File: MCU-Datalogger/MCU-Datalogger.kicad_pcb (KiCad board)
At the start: 2 copper layers, 29 parts, among them J1 Conn_01x04_Pin, J2 Conn_01x04_Pin, J3 Conn_01x09_Pin, J4 Conn_02x03_Odd_Even, U1 24LC1025, U2 24LC1025, U3 DS1337S+, U4 ATMEGA328P-AU, Y1 32.768 KHz, Y2 16 MHz

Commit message: Added Outline in Edge.Cuts
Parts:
- moved H1 42.0 mm to (186.7, 81.8)
- moved H2 42.0 mm to (186.7, 87.6)
- moved H3 42.0 mm to (186.7, 93.3)
- moved H4 42.0 mm to (186.7, 99.1)
- moved C2 29.1 mm to (219.7, 95.5)
- moved C5 29.1 mm to (219.7, 104.5)
- moved D1 29.1 mm to (224.1, 99.7)
- moved D2 29.1 mm to (224.1, 102.8)
- moved R2 29.1 mm to (204.9, 83.4)
- moved R3 29.1 mm to (204.9, 86.3)
- moved R7 29.1 mm to (204.9, 98.1)
- moved U1 29.1 mm to (212.3, 94.4)
- moved U2 29.1 mm to (212.3, 101.2)
- moved C1 29.1 mm to (219.7, 92.5)
- moved C3 29.1 mm to (219.7, 98.5)
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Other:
- board outline added: 50.8 x 30.5 mm

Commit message: Place components
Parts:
- moved J3 99.7 mm to (134.0, 103.5), turned to 90 degrees
- moved BT1 92.5 mm to (132.1, 85.1)
- moved U3 84.2 mm to (139.7, 94.6)
- moved J2 84.0 mm to (159.4, 103.5), turned to 90 degrees
- moved Y1 80.9 mm to (132.1, 95.9), turned to 90 degrees
- moved U2 75.4 mm to (139.7, 80.6)
- moved C1 73.6 mm to (147.3, 78.7)
- moved U1 72.9 mm to (139.7, 87.6)
- moved C3 71.3 mm to (151.1, 78.7)
- moved R1 69.6 mm to (137.8, 99.1)
- moved C5 68.5 mm to (156.2, 78.7)
- moved D1 66.0 mm to (161.6, 78.7)
- moved J4 65.8 mm to (170.8, 83.2)
- moved R2 65.2 mm to (141.6, 99.1), turned to 180 degrees
- moved J1 63.4 mm to (173.4, 92.1)
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
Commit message: Refine outline
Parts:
- moved H3 1.61 mm to (130.0, 105.7)
- moved H4 1.52 mm to (175.3, 105.7)
- moved H1 1.14 mm to (130.0, 77.7)
- moved H2 1.02 mm to (175.3, 77.7)
- moved J3 0.65 mm to (134.6, 103.6)
- moved J2 0.64 mm to (160.0, 103.5)
- moved C1 0.34 mm to (147.6, 78.9)
- moved C3 0.32 mm to (151.4, 78.9)
- moved D1 0.31 mm to (161.8, 78.9)
- moved D2 0.31 mm to (166.0, 78.9)
- moved C5 0.30 mm to (156.5, 78.9)
- moved U2 0.13 mm to (139.7, 80.8)
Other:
- board size 50.8 x 30.5 mm -> 51.3 x 34 mm
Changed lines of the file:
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@@
   )
   (footprint "Package_SO:SOIC-8_5.23x5.23mm_P1.27mm" (layer "F.Cu")
-    (at 139.7 80.645)
+    (at 139.7254 80.7724)
     (descr "SOIC, 8 Pin (http://www.winbond.com/resource-files/w25q32jv%20revg%2003272018%20plus.pdf#page=68), generated with kicad-footprint-generator ipc_gullwing_generator.py")
     (tags "SOIC SO")
@@
     (property "ki_keywords" "I2C Serial EEPROM")
     (attr smd)
-    (fp_text reference "U2" (at 0 -3.56) (layer "F.SilkS")
+    (fp_text reference "U2" (at 0.3025 -3.56) (layer "F.SilkS")
         (effects (font (size 1 1) (thickness 0.15)))
     )
@@
   )
   (footprint "Connector_PinHeader_2.54mm:PinHeader_1x04_P2.54mm_Vertical" (layer "F.Cu")
-    (at 159.385 103.505 90)
+    (at 160.02 103.505 90)
     (descr "Through hole straight pin header, 1x04, 2.54mm pitch, single row")
     (tags "Through hole pin header THT 1x04 2.54mm single row")
@@
   )
   (footprint "LED_SMD:LED_0805_2012Metric" (layer "F.Cu")
-    (at 161.5675 78.74)
+    (at 161.8238 78.9074)
     (descr "LED SMD 0805 (2012 Metric), square (rectangular) end terminal, IPC_7351 nominal, (Body size source: https://docs.google.com/spreadsheets/d/1BsfQQcO9C6DZCsRaXUlFlo91Tg2WpOkGARC1WS5S8t0/edit?usp=sharing), generated with kicad-footprint-generator")
     (tags "LED")
@@
   )
   (footprint "Capacitor_SMD:C_0805_2012Metric" (layer "F.Cu")
-    (at 156.21 78.74)
+    (at 156.464 78.8924)
     (descr "Capacitor SMD 0805 (2012 Metric), square (rectangular) end terminal, IPC_7351 nominal, (Body size source: IPC-SM-782 page 76, https://www.pcb-3d.com/wordpress/wp-content/uploads/ipc-sm-782a_amendment_1_and_2.pdf, https://docs.google.com/spreadsheets/d/1BsfQQcO9C6DZCsRaXUlFlo91Tg2WpOkGARC1WS5S8t0/edit?usp=sharing), generated with kicad-footprint-generator")
     (tags "capacitor")
@@
   )
   (footprint "Connector_PinHeader_2.54mm:PinHeader_1x09_P2.54mm_Vertical" (layer "F.Cu")
-    (at 133.985 103.505 90)
+    (at 134.62 103.632 90)
     (descr "Through hole straight pin header, 1x09, 2.54mm pitch, single row")
     (tags "Through hole pin header THT 1x09 2.54mm single row")
@@
   )
   (footprint "MountingHole:MountingHole_2.1mm" (layer "F.Cu")
-    (at 129.54 104.14)
+    (at 130.048 105.664)
     (descr "Mounting Hole 2.1mm, no annular")
     (tags "mounting hole 2.1mm no annular")
@@
   )
   (footprint "LED_SMD:LED_0805_2012Metric" (layer "F.Cu")
-    (at 165.735 78.74)
+    (at 165.9913 78.9074)
     (descr "LED SMD 0805 (2012 Metric), square (rectangular) end terminal, IPC_7351 nominal, (Body size source: https://docs.google.com/spreadsheets/d/1BsfQQcO9C6DZCsRaXUlFlo91Tg2WpOkGARC1WS5S8t0/edit?usp=sharing), generated with kicad-footprint-generator")
     (tags "LED")
@@
   )
   (footprint "MountingHole:MountingHole_2.1mm" (layer "F.Cu")
-    (at 175.26 104.14)
+    (at 175.26 105.664)
     (descr "Mounting Hole 2.1mm, no annular")
     (tags "mounting hole 2.1mm no annular")
@@
   )
   (footprint "Capacitor_SMD:C_0805_2012Metric" (layer "F.Cu")
-    (at 147.32 78.74)
+    (at 147.6248 78.8924)
     (descr "Capacitor SMD 0805 (2012 Metric), square (rectangular) end terminal, IPC_7351 nominal, (Body size source: IPC-SM-782 page 76, https://www.pcb-3d.com/wordpress/wp-content/uploads/ipc-sm-782a_amendment_1_and_2.pdf, https://docs.google.com/spreadsheets/d/1BsfQQcO9C6DZCsRaXUlFlo91Tg2WpOkGARC1WS5S8t0/edit?usp=sharing), generated with kicad-footprint-generator")
     (tags "capacitor")
@@
   )
   (footprint "MountingHole:MountingHole_2.1mm" (layer "F.Cu")
-    (at 129.54 78.74)
+    (at 130.048 77.724)
     (descr "Mounting Hole 2.1mm, no annular")
     (tags "mounting hole 2.1mm no annular")
@@
   )
   (footprint "MountingHole:MountingHole_2.1mm" (layer "F.Cu")
-    (at 175.26 78.74)
+    (at 175.26 77.724)
     (descr "Mounting Hole 2.1mm, no annular")
     (tags "mounting hole 2.1mm no annular")
@@
   )
   (footprint "Capacitor_SMD:C_0805_2012Metric" (layer "F.Cu")
-    (at 151.13 78.74)
+    (at 151.4094 78.8924)
     (descr "Capacitor SMD 0805 (2012 Metric), square (rectangular) end terminal, IPC_7351 nominal, (Body size source: IPC-SM-782 page 76, https://www.pcb-3d.com/wordpress/wp-content/uploads/ipc-sm-782a_amendment_1_and_2.pdf, https://docs.google.com/spreadsheets/d/1BsfQQcO9C6DZCsRaXUlFlo91Tg2WpOkGARC1WS5S8t0/edit?usp=sharing), generated with kicad-footprint-generator")
     (tags "capacitor")
@@
     )
   )
-  (gr_rect (start 127 76.2) (end 177.8 106.68)
-    (stroke (width 0.1) (type default)) (fill none) (layer "Edge.Cuts"))
+  (gr_line (start 133.096 105.664) (end 172.212 105.664)
+    (stroke (width 0.1) (type default)) (layer "Edge.Cuts"))
+  (gr_line (start 175.26 101.6) (end 175.26 80.772)
+    (stroke (width 0.1) (type default)) (layer "Edge.Cuts"))
+  (gr_line (start 130.048 80.772) (end 130.048 102.616)
+    (stroke (width 0.1) (type default)) (layer "Edge.Cuts"))
+  (gr_arc (start 130.048 80.772) (mid 127.892739 75.568739) (end 133.096 77.724)
+    (stroke (width 0.1) (type default)) (layer "Edge.Cuts"))
+  (gr_line (start 172.212 77.724) (end 133.096 77.724)
+    (stroke (width 0.1) (type default)) (layer "Edge.Cuts"))
+  (gr_arc (start 172.212 77.724) (mid 177.415261 75.568739) (end 175.26 80.772)
+    (stroke (width 0.1) (type default)) (layer "Edge.Cuts"))
+  (gr_arc (start 133.096 105.664) (mid 127.892739 107.819261) (end 130.048 102.616)
+    (stroke (width 0.1) (type default)) (layer "Edge.Cuts"))
+  (gr_line (start 175.26 102.616) (end 175.26 101.6)
+    (stroke (width 0.1) (type default)) (layer "Edge.Cuts"))
+  (gr_arc (start 175.26 102.616) (mid 177.415261 107.819261) (end 172.212 105.664)
+    (stroke (width 0.1) (type default)) (layer "Edge.Cuts"))
 )

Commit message: Roututing
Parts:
- turned C1 to 180 degrees
- turned Y2 to 180 degrees
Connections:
- D2 pad 2: Net-(D2-A) -> /SCK
- U4 pad 17: Net-(D2-A) -> /SCK
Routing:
- net /Vcc: track 0.00 -> 104.3 mm, vias 0 -> 1
- net /SCK: track 0.00 -> 102.1 mm, vias 0 -> 3
- net Net-(BT1-+): track 0.00 -> 57.7 mm, vias 0 -> 5
- net /SDA: track 0.00 -> 57.7 mm, vias 0 -> 2
- net GND: track 0.00 -> 48.3 mm, vias 0 -> 6
- net Net-(U4-PB7): track 0.00 -> 31.2 mm, vias 0 -> 2
- net /TX: track 0.00 -> 30.4 mm, vias 0 -> 1
- net /D2: track 0.00 -> 28.6 mm, vias 0 -> 1
- net /RX: track 0.00 -> 28.3 mm, vias 0 -> 1
- net /D3: track 0.00 -> 26.0 mm
- net Net-(U4-PB6): track 0.00 -> 25.4 mm
- net /MOSI: track 0.00 -> 24.8 mm
- net /RESET: track 0.00 -> 24.3 mm, vias 0 -> 4
- net /D4: track 0.00 -> 22.7 mm
- net /MISO: track 0.00 -> 20.2 mm, vias 0 -> 1
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
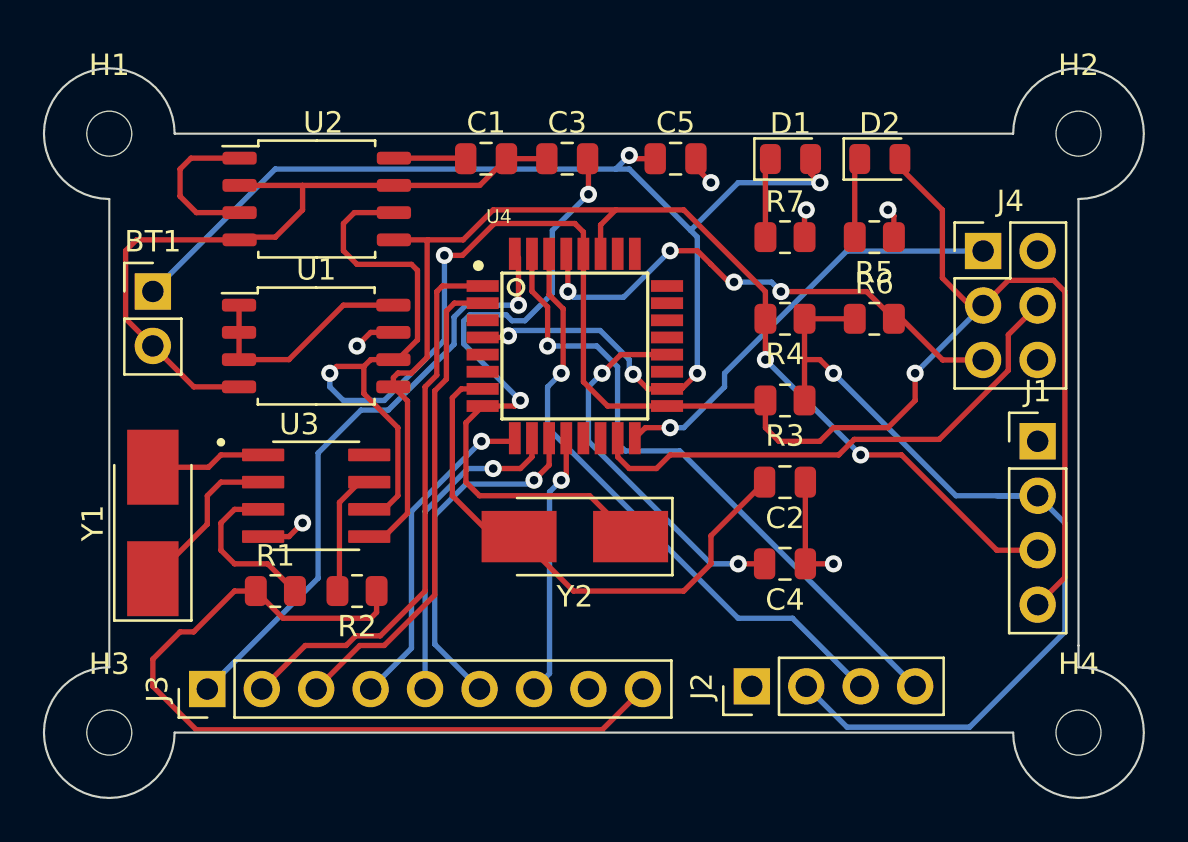
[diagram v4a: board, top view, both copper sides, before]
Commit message: refine silkscreen
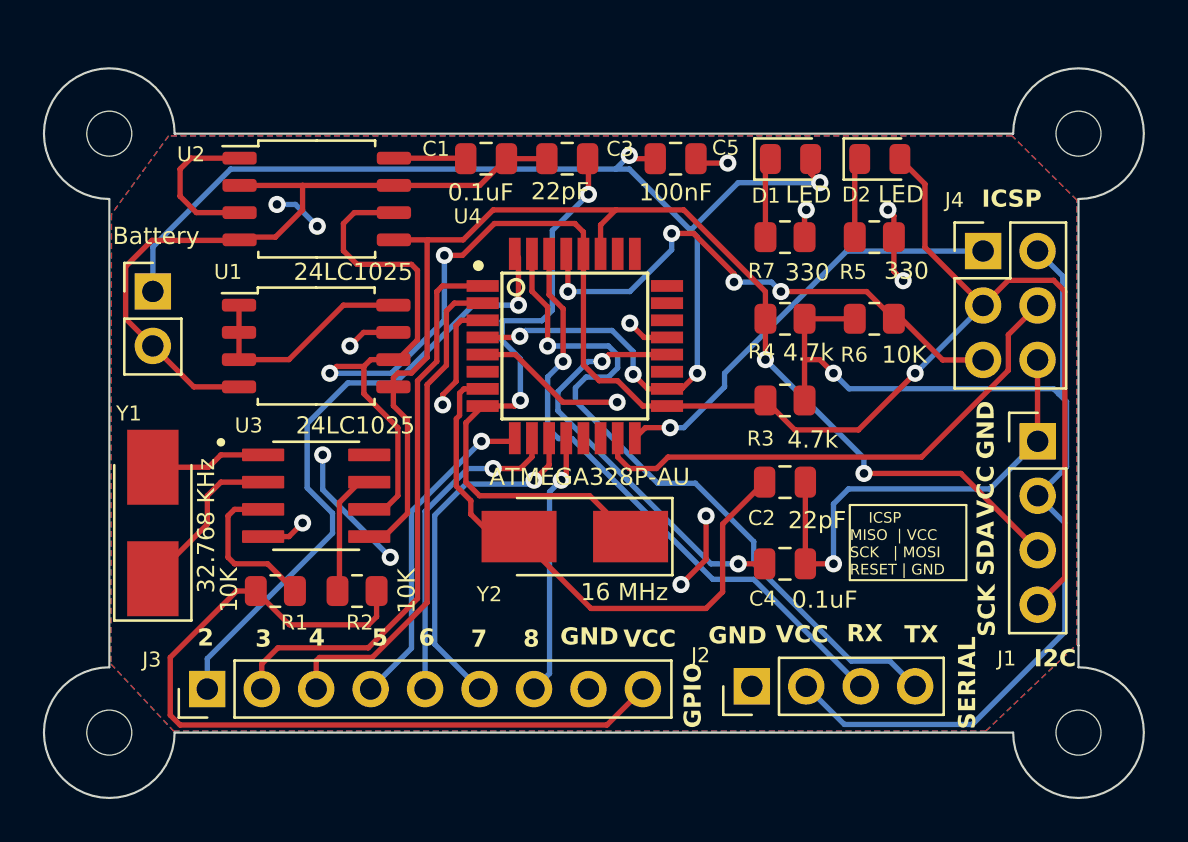
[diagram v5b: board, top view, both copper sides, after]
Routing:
- net GND: track 48.3 -> 86.1 mm, vias 6 -> 12
- net /Vcc: track 104.3 -> 121.8 mm, vias 1 -> 5
- net /SCK: track 102.1 -> 97.4 mm
- net /TX: track 30.4 -> 33.6 mm
- net Net-(U4-PB7): track 31.2 -> 28.9 mm
- net Net-(U4-AREF): track 17.4 -> 19.3 mm
- net Net-(BT1-+): track 57.7 -> 59.3 mm
- net Net-(U4-PB6): track 25.4 -> 27.0 mm
- net /D2: track 28.6 -> 29.9 mm
- net /RESET: track 24.3 -> 25.4 mm
- net /D4: track 22.7 -> 23.4 mm
- net /D3: track 26.0 -> 26.6 mm
- added copper zone on F.Cu, net /Vcc
- added copper zone on B.Cu, net GND
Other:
- board text added: "2"
- board text added: "3"
- board text added: "4"
- board text added: "5"
- board text added: "6"
- board text added: "7"
- board text added: "8"
- board text added: "GND"
- board text added: "GPIO"
- board text added: "I2C"
- board text added: "ICSP"
- board text added: "ICSP MISO | VCC SCK | MOSI RESET | GND"
- board text added: "RX"
- board text added: "SCK"
- board text added: "SDA"
- board text added: "SERIAL"
- board text added: "TX"
- board text added: "VCC"

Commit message: fixed outstanding issues
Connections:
- BT1 pad 1: Net-(BT1-+) -> /Vcc
- C5 pad 1: Net-(BT1-+) -> /Vcc
- D1 pad 2: Net-(BT1-+) -> /Vcc
- U4 pad 18: Net-(BT1-+) -> /Vcc
- U4 pad 4: Net-(BT1-+) -> /Vcc
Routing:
- net /Vcc: track 121.8 -> 181.1 mm, vias 5 -> 10
- net Net-(BT1-+): track 59.3 -> 0.00 mm, vias 5 -> 0
- net GND: track 86.1 -> 103.0 mm, vias 12 -> 14
- net Net-(U4-PB7): track 28.9 -> 27.6 mm
- net Net-(U4-PB6): track 27.0 -> 26.1 mm
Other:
- board text added: "Datalogger with the ATMega328P"

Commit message: generate gebers files
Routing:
- net GND: track 103.0 -> 101.7 mm
- net /SDA: track 57.7 -> 58.9 mm
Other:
- board text added: "0.2000 mm / 0.0000 mm"
- board text added: "0.3000 mm"
- board text added: "1.6000 mm"
- board text added: "51.3035 mm x 34.0315 mm"
- board text added: "BOARD CHARACTERISTICS"
- board text added: "Board Thickness:"
- board text added: "Board overall dimensions:"
- board text added: "Castellated pads:"
- board text added: "Copper Finish:"
- board text added: "Copper Layer Count:"
- board text added: "Edge card connectors:"
- board text added: "Impedance Control:"
- board text added: "Min hole diameter:"
- board text added: "Min track/spacing:"
- board text added: "No"
- board text added: "None"
- board text added: "Plated Board Edge:"
